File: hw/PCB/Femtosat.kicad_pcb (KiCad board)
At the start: 2 copper layers, 105 x 54 mm, 39 parts, among them J1 USB_B_Micro, J2 Programmer, J4 Battery, J5 Micro_SD_Card_Det, SW1 Reset_push, U1 AP7215-33YG-13, U2 AV4524, U3 LP38693MP-5.0, U4 TRH-G2, U5 NRF24L01_Breakout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

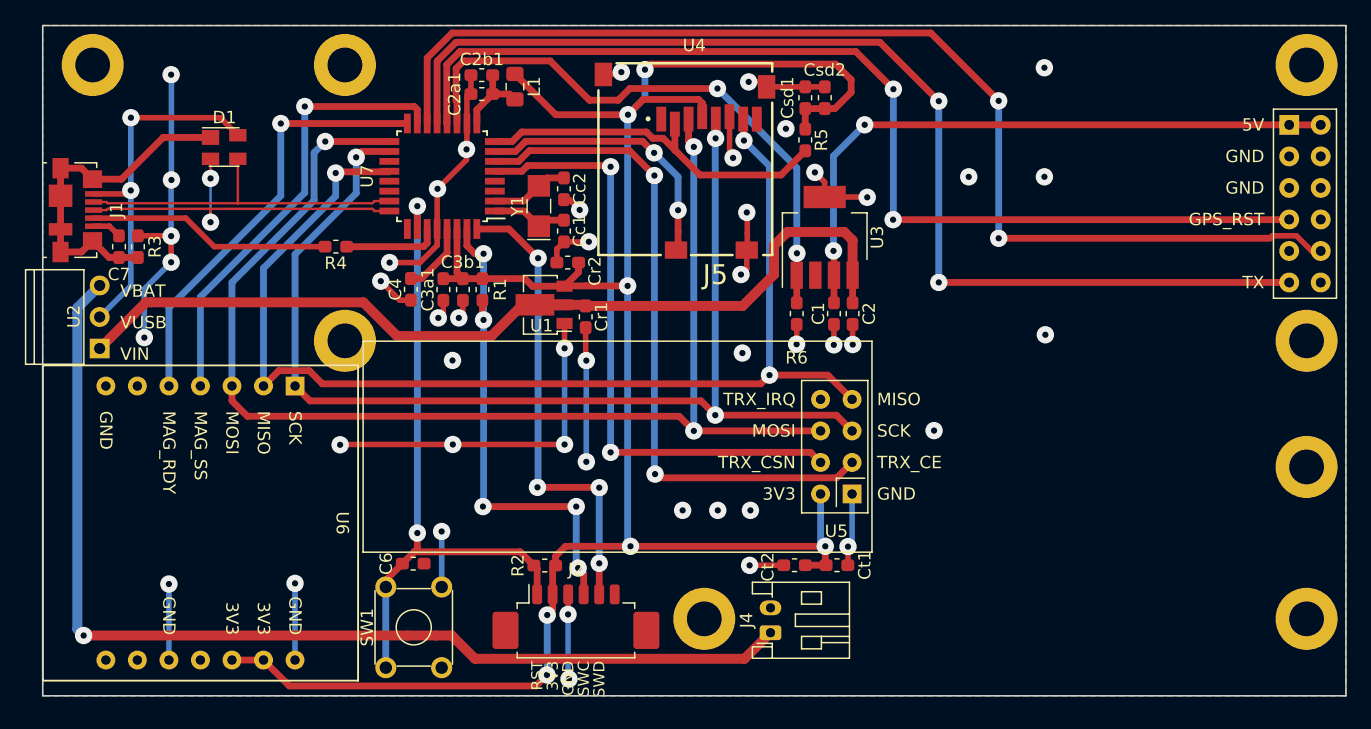
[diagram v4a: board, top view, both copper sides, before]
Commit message: Modified the design of the femto-satellite. Now it is smaller an it has a temperature sensor to calibrate the magnetometer.
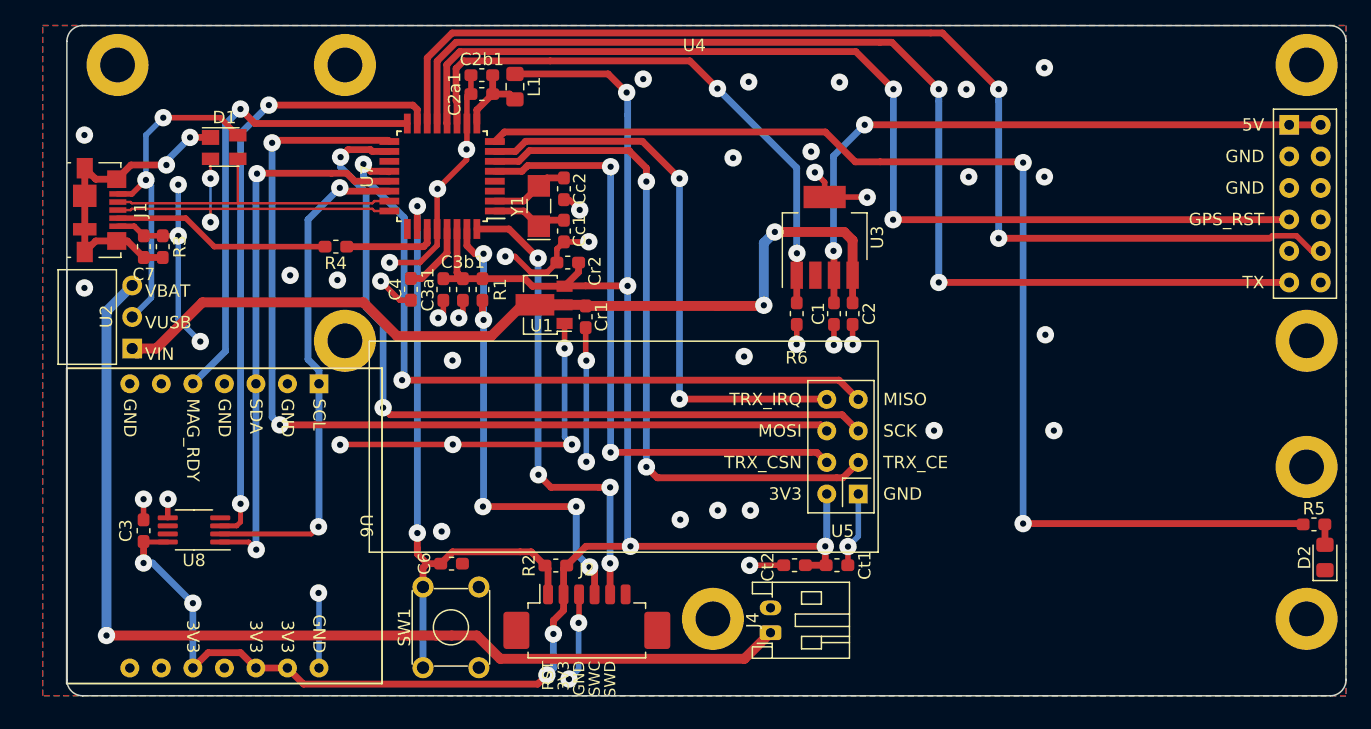
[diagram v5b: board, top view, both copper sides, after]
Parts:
- removed Csd1: 10uF, Capacitor_SMD:C_0603_1608Metric_Pad1.05x0.95mm_HandSolder
- removed Csd2: 100nF, Capacitor_SMD:C_0603_1608Metric_Pad1.05x0.95mm_HandSolder
- removed J5: Micro_SD_Card_Det, SD:GCT_MEM2061-01-188-00-A_REVA
- added C3: 100nF, Capacitor_SMD:C_0603_1608Metric_Pad1.05x0.95mm_HandSolder, F.Cu at (74.5, 70.2)
- added D2: LED, LED_SMD:LED_0805_2012Metric_Pad1.15x1.40mm_HandSolder, F.Cu at (169.7, 72.3)
- added U8: MCP9808-EMS, Package_SO:MSOP-8_3x3mm_P0.65mm, F.Cu at (78.5, 70.1)
- R5: value 100k -> 330
- moved R5 51.4 mm to (168.8, 69.7), turned to 0 degrees
- moved C6 3.08 mm to (99.3, 72.8)
- moved SW1 2.99 mm to (97.0, 81.2)
- moved U2 2.62 mm to (73.6, 53.0)
- moved C7 2.00 mm to (74.5, 47.3)
- moved R3 2.00 mm to (76.0, 47.3)
- moved J1 1.95 mm to (71.0, 44.3)
- moved U6 1.94 mm to (81.0, 69.8)
- moved R2 0.89 mm to (107.7, 73.0)
- moved J2 0.88 mm to (110.2, 77.7)
- moved U5 0.50 mm to (132.1, 67.2)
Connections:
- R5 pad 1: +3V3 -> /STS_LED
- R5 pad 2: /DL_NSS -> Net-(D2-Pad2)
- U6 pad 1: /SCK -> /SCL
- U6 pad 10: GND -> +3V3
- U6 pad 2: /MISO -> GND
- U6 pad 3: /MOSI -> /SDA
- U6 pad 4: /MAG_SS -> GND
- U7 pad 15: /MAG_SS -> /T_ALERT
- U7 pad 7: /DL_CD -> /TRX_IRQ
- U7 pad 8: /DL_NSS -> /STS_LED
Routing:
- net /STS_LED: track 0.00 -> 96.1 mm, vias 0 -> 2
- net /T_ALERT: track 0.00 -> 49.5 mm, vias 0 -> 2
- net /TRX_IRQ: track 0.00 -> 46.1 mm, vias 0 -> 2
- net /SDA: track 0.00 -> 44.4 mm, vias 0 -> 2
- net /SCL: track 0.00 -> 41.0 mm, vias 0 -> 2
- net /MISO: track 95.8 -> 59.4 mm, vias 3 -> 2
- net /MAG_SS: track 36.3 -> 0.00 mm, vias 1 -> 0
- net /DL_NSS: track 31.0 -> 0.00 mm
- net /SCK: track 94.0 -> 64.9 mm, vias 3 -> 2
- net /MOSI: track 102.9 -> 76.8 mm, vias 3 -> 2
- net GND: track 156.3 -> 131.0 mm, vias 47 -> 52
- net /DL_CD: track 22.3 -> 0.00 mm, vias 2 -> 0
- net +3V3: track 168.9 -> 151.6 mm, vias 7 -> 8
- net /VUSB: track 29.4 -> 26.8 mm
- net /MAG_RDY: track 35.1 -> 37.7 mm
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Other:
- board size 105 x 54 mm -> 103.1 x 54 mm
- board text added: "...puestos los ojos en Jesús, el autor y consumador de la fe, el cual por el gozo puesto delante de él sufrió la cruz, menospreciando el oprobio, y se sentó a la diestra del trono de Dios."
- board text added: "FE v3.2201"
- board text added: "SCL"
- board text added: "SDA"
- board text removed: "FE v3.2110"
- board text removed: "MAG_SS"
